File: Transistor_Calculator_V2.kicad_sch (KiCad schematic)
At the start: 51 parts, among them Q1 2N3904, Q10 2N3904, Q11 2N3904, Q12 2N3904, Q13 2N3904, Q14 2N3904, Q15 2N3904, Q16 2N3904, Q17 2N3904, Q18 2N3904, Q19 2N3904, Q2 2N3904, Q3 2N3904, Q4 2N3904, Q5 2N3904, Q6 2N3904, Q7 2N3904, Q8 2N3904, Q9 2N3904

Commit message: update transistors
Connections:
- net GND: now also Q1.1 (E), Q10.1 (E), Q12.1 (E), Q13.1 (E), Q15.1 (E), Q16.1 (E), Q17.1 (E), Q18.1 (E), Q19.1 (E), Q4.1 (E), Q5.1 (E), Q6.1 (E), Q9.1 (E)
- net Vcc: now also R12.2, R14.2, R15.1, R16.2, R17.2, R20.2, R23.2, R24.2, R27.2, R28.2, R4.2, R5.2, R7.2, R8.2
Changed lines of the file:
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@@
 	)
 	(junction
+		(at 127 31.75)
+		(diameter 0)
+		(color 0 0 0 0)
+	)
+	(junction
 		(at 236.22 133.35)
 		(diameter 0)
@@
 	)
 	(junction
+		(at 132.08 191.77)
+		(diameter 0)
+		(color 0 0 0 0)
+	)
+	(junction
 		(at 72.39 85.09)
 		(diameter 0)
@@
 	(wire
 		(pts
+			(xy 127 20.32) (xy 127 31.75)
+		)
+		(stroke
+			(width 0)
+			(type default)
+		)
+	)
+	(wire
+		(pts
 			(xy 58.42 157.48) (xy 58.42 162.56)
 		)
@@
 	(wire
 		(pts
+			(xy 132.08 191.77) (xy 121.92 191.77)
+		)
+		(stroke
+			(width 0)
+			(type default)
+		)
+	)
+	(wire
+		(pts
 			(xy 43.18 167.64) (xy 31.75 167.64)
 		)
@@
 	(wire
 		(pts
-			(xy 175.26 191.77) (xy 121.92 191.77)
+			(xy 175.26 191.77) (xy 132.08 191.77)
 		)
 		(stroke
@@
 	(wire
 		(pts
-			(xy 121.92 31.75) (xy 186.69 31.75)
+			(xy 121.92 31.75) (xy 127 31.75)
 		)
 		(stroke
@@
 	(wire
 		(pts
+			(xy 132.08 191.77) (xy 132.08 195.58)
+		)
+		(stroke
+			(width 0)
+			(type default)
+		)
+	)
+	(wire
+		(pts
+			(xy 135.89 20.32) (xy 127 20.32)
+		)
+		(stroke
+			(width 0)
+			(type default)
+		)
+	)
+	(wire
+		(pts
 			(xy 121.92 182.88) (xy 121.92 191.77)
 		)
@@
 	(wire
 		(pts
+			(xy 127 31.75) (xy 186.69 31.75)
+		)
+		(stroke
+			(width 0)
+			(type default)
+		)
+	)
+	(wire
+		(pts
 			(xy 161.29 85.09) (xy 179.07 85.09)
 		)
@@
 	(wire
 		(pts
+			(xy 143.51 195.58) (xy 132.08 195.58)
+		)
+		(stroke
+			(width 0)
+			(type default)
+		)
+	)
+	(wire
+		(pts
 			(xy 91.44 39.37) (xy 100.33 39.37)
 		)
@@
 		)
 	)
+	(global_label "Vcc"
+		(shape input)
+		(at 135.89 20.32 0)
+		(fields_autoplaced yes)
+		(effects
+			(font
+				(size 1.27 1.27)
+			)
+			(justify left)
+		)
+		(property "Intersheetrefs" "${INTERSHEET_REFS}"
+			(at 142.141 20.32 0)
+			(effects
+				(font
+					(size 1.27 1.27)
+				)
+				(justify left)
+				(hide yes)
+			)
+		)
+	)
 	(symbol
 		(lib_id "Transistor_BJT:2N3904")
@@
 			)
 		)
-		(property "Sim.Pins" "1=C 2=B 3=E"
+		(property "Sim.Pins" "1=E 2=B 3=C"
 			(at 69.85 41.91 0)
 			(effects
@@
 	)
 	(symbol
+		(lib_id "power:GND")
+		(at 143.51 195.58 90)
+		(unit 1)
+		(exclude_from_sim no)
+		(in_bom yes)
+		(on_board yes)
+		(dnp no)
+		(fields_autoplaced yes)
+		(property "Reference" "#PWR05"
+			(at 149.86 195.58 0)
+			(effects
+				(font
+					(size 1.27 1.27)
+				)
+				(hide yes)
+			)
+		)
+		(property "Value" "GND"
+			(at 148.59 195.58 0)
+			(effects
+				(font
+					(size 1.27 1.27)
+				)
+			)
+		)
+		(property "Footprint" ""
+			(at 143.51 195.58 0)
+			(effects
+				(font
+					(size 1.27 1.27)
+				)
+				(hide yes)
+			)
+		)
+		(property "Datasheet" ""
+			(at 143.51 195.58 0)
+			(effects
+				(font
+					(size 1.27 1.27)
+				)
+				(hide yes)
+			)
+		)
+		(property "Description" "Power symbol creates a global label with name \"GND\" , ground"
+			(at 143.51 195.58 0)
+			(effects
+				(font
+					(size 1.27 1.27)
+				)
+				(hide yes)
+			)
+		)
+		(pin "1"
+		)
+		(instances
+			(project "Transistor_Calculator_V2"
+				(path "/4e74c2aa-3410-4407-95d8-73d62854742b"
+					(reference "#PWR05")
+					(unit 1)
+				)
+			)
+		)
+	)
+	(symbol
 		(lib_id "Transistor_BJT:2N3904")
 		(at 55.88 167.64 0)
@@
 			)
 		)
-		(property "Sim.Pins" "1=C 2=B 3=E"
+		(property "Sim.Pins" "1=E 2=B 3=C"
 			(at 69.85 80.01 0)
 			(effects

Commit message: renamed vinc
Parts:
- Vin1: value 0 -> 5
- renumbered Vinc1 to Vinc
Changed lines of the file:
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@@
 			)
 		)
-		(property "Value" "0"
+		(property "Value" "5"
 			(at -68.58 101.4701 0)
 			(effects
@@
 		(dnp no)
 		(fields_autoplaced yes)
-		(property "Reference" "Vinc1"
+		(property "Reference" "Vinc"
 			(at -36.83 98.9301 0)
 			(effects
@@
 			(project "Transistor_Calculator_V2"
 				(path "/4e74c2aa-3410-4407-95d8-73d62854742b"
-					(reference "Vinc1")
-					(unit 1)
-				)
+					(reference "Vinc")
+					(unit 1)
+				)

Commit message: Fixed the carry bit problem for the schematic
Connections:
- net Vo2: no longer Q13.3 (C), Q16.3 (C), R16.1, R24.1, R25.1, R26.1
- new net: Q16.3 (C), R24.1, R25.1
- new net: Q13.3 (C), R16.1, R26.1
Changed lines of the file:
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@@
-	)
-	(junction
-		(at 165.1 135.89)
-		(diameter 0)
-		(color 0 0 0 0)
 	)
 	(junction
@@
 	)
 	(junction
-		(at 153.67 156.21)
-		(diameter 0)
-		(color 0 0 0 0)
-	)
-	(junction
 		(at 100.33 85.09)
 		(diameter 0)
@@
 	)
 	(junction
-		(at 152.4 144.78)
-		(diameter 0)
-		(color 0 0 0 0)
-	)
-	(junction
 		(at 72.39 50.8)
 		(diameter 0)
@@
 	)
 	(junction
-		(at 236.22 133.35)
-		(diameter 0)
-		(color 0 0 0 0)
-	)
-	(junction
 		(at 58.42 162.56)
 		(diameter 0)
@@
 	(wire
 		(pts
-			(xy 152.4 144.78) (xy 175.26 144.78)
+			(xy 143.51 144.78) (xy 175.26 144.78)
 		)
 		(stroke
@@
 	(wire
 		(pts
-			(xy 152.4 144.78) (xy 152.4 142.24)
-		)
-		(stroke
-			(width 0)
-			(type default)
-		)
-	)
-	(wire
-		(pts
 			(xy 107.95 85.09) (xy 161.29 85.09)
 		)
@@
 	(wire
 		(pts
-			(xy 143.51 144.78) (xy 152.4 144.78)
-		)
-		(stroke
-			(width 0)
-			(type default)
-		)
-	)
-	(wire
-		(pts
-			(xy 165.1 121.92) (xy 236.22 121.92)
-		)
-		(stroke
-			(width 0)
-			(type default)
-		)
-	)
-	(wire
-		(pts
 			(xy 254 39.37) (xy 254 113.03)
 		)
@@
 	(wire
 		(pts
-			(xy 170.18 142.24) (xy 170.18 135.89)
-		)
-		(stroke
-			(width 0)
-			(type default)
-		)
-	)
-	(wire
-		(pts
 			(xy 252.73 115.57) (xy 252.73 133.35)
 		)
@@
 	(wire
 		(pts
-			(xy 236.22 121.92) (xy 236.22 133.35)
-		)
-		(stroke
-			(width 0)
-			(type default)
-		)
-	)
-	(wire
-		(pts
 			(xy 190.5 134.62) (xy 190.5 138.43)
 		)
@@
 	(wire
 		(pts
-			(xy 165.1 121.92) (xy 165.1 135.89)
-		)
-		(stroke
-			(width 0)
-			(type default)
-		)
-	)
-	(wire
-		(pts
 			(xy 190.5 161.29) (xy 201.93 161.29)
 		)
@@
 	(wire
 		(pts
-			(xy 151.13 156.21) (xy 151.13 135.89)
-		)
-		(stroke
-			(width 0)
-			(type default)
-		)
-	)
-	(wire
-		(pts
 			(xy 198.12 39.37) (xy 198.12 54.61)
 		)
@@
 	(wire
 		(pts
-			(xy 215.9 133.35) (xy 236.22 133.35)
+			(xy 215.9 133.35) (xy 252.73 133.35)
 		)
 		(stroke
@@
 	(wire
 		(pts
-			(xy 236.22 133.35) (xy 252.73 133.35)
-		)
-		(stroke
-			(width 0)
-			(type default)
-		)
-	)
-	(wire
-		(pts
 			(xy 127 72.39) (xy 127 105.41)
 		)
@@
 	(wire
 		(pts
-			(xy 153.67 156.21) (xy 151.13 156.21)
-		)
-		(stroke
-			(width 0)
-			(type default)
-		)
-	)
-	(wire
-		(pts
 			(xy 180.34 38.1) (xy 180.34 39.37)
 		)
@@
 	(wire
 		(pts
-			(xy 151.13 135.89) (xy 165.1 135.89)
-		)
-		(stroke
-			(width 0)
-			(type default)
-		)
-	)
-	(wire
-		(pts
 			(xy 207.01 44.45) (xy 207.01 39.37)
 		)
@@
 	(wire
 		(pts
-			(xy 165.1 135.89) (xy 170.18 135.89)
-		)
-		(stroke
-			(width 0)
-			(type default)
-		)
-	)
-	(wire
-		(pts
 			(xy 170.18 50.8) (xy 170.18 54.61)
 		)
@@
 		)
 		(stroke
-			(width 0)
-			(type default)
-		)
-	)
-	(wire
-		(pts
-			(xy 152.4 142.24) (xy 170.18 142.24)
-		)
-		(stroke

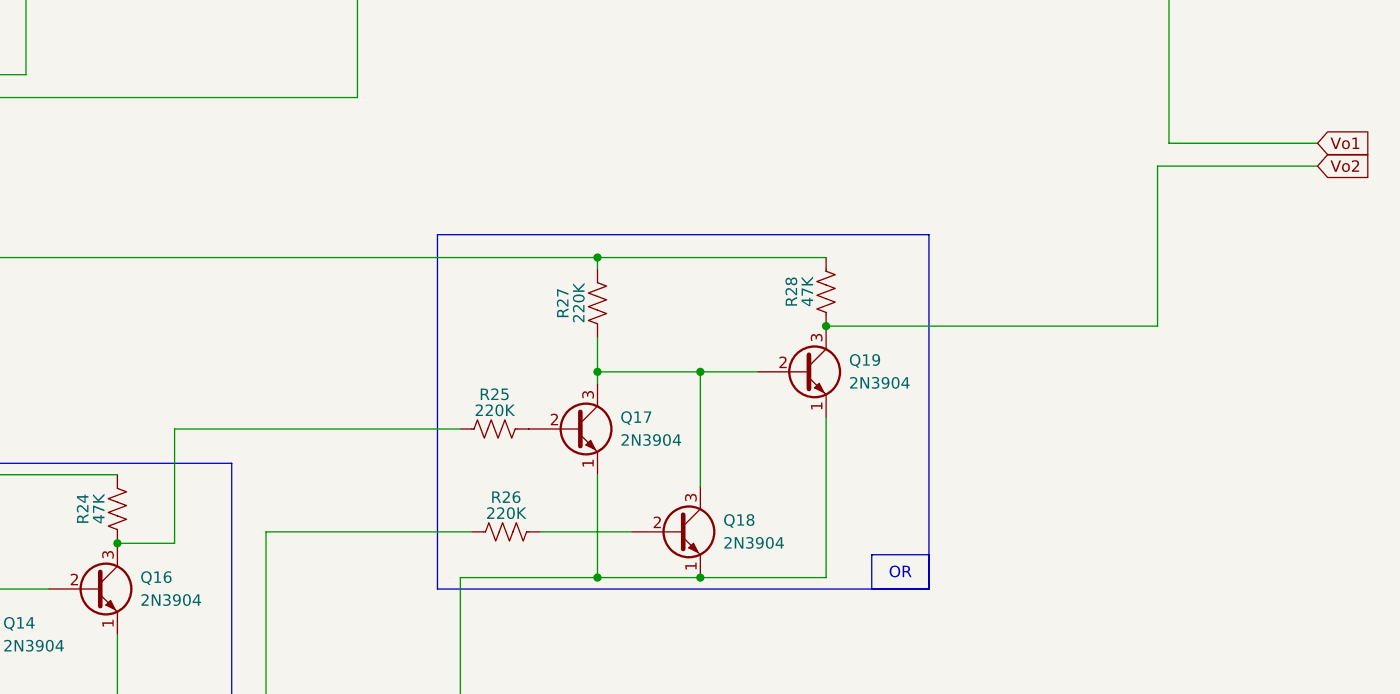
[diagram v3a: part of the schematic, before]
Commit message: Added diode to replace OR gate
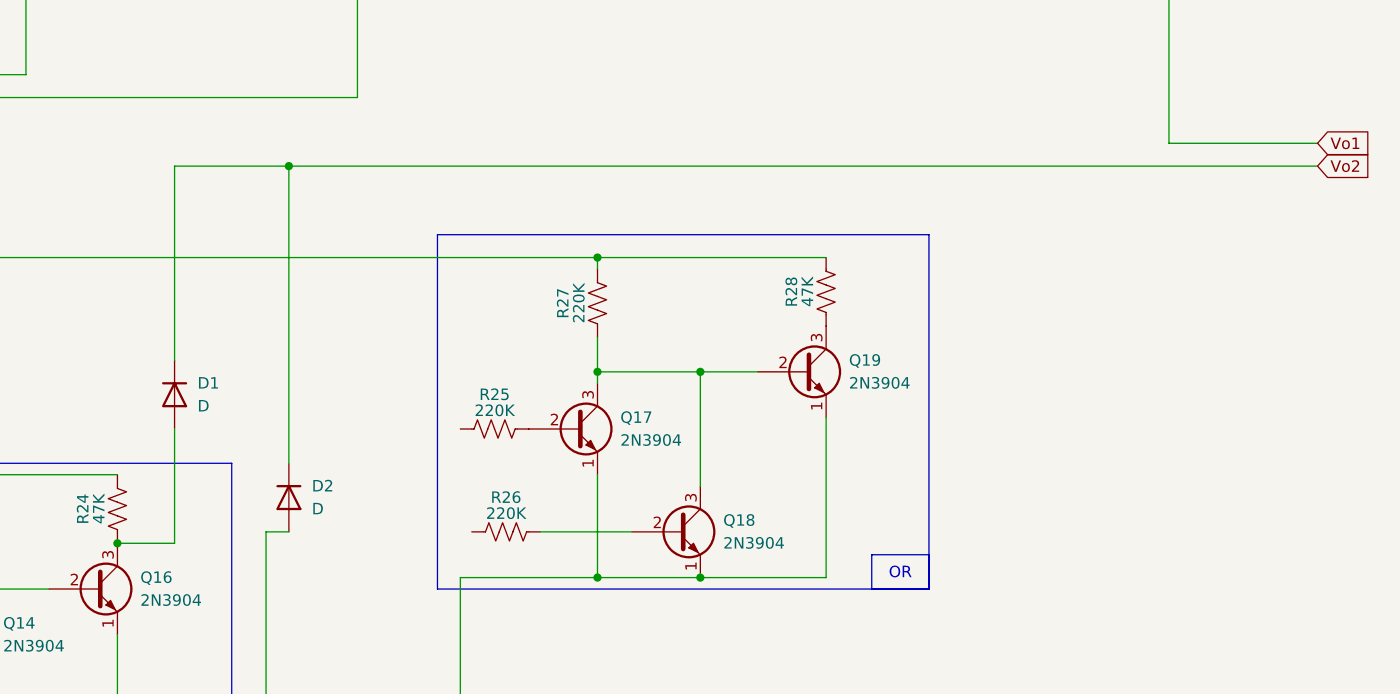
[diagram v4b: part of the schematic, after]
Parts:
- added D1, D2: D, symbol Device:D
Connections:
- net Vo2: now also D1.1 (K), D2.1 (K); no longer Q19.3 (C), R28.1
- net at Q16.3 (C), R24.1: now also D1.2 (A); no longer R25.1
- net at Q13.3 (C), R16.1: now also D2.2 (A); no longer R26.1
- new net: Q19.3 (C), R28.1
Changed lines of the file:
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@@
 	)
 	(junction
+		(at 156.21 115.57)
+		(diameter 0)
+		(color 0 0 0 0)
+	)
+	(junction
 		(at 161.29 85.09)
 		(diameter 0)
@@
 	)
 	(junction
-		(at 215.9 133.35)
-		(diameter 0)
-		(color 0 0 0 0)
-	)
-	(junction
 		(at 198.12 39.37)
 		(diameter 0)
@@
 	(wire
 		(pts
-			(xy 143.51 144.78) (xy 175.26 144.78)
-		)
-		(stroke
-			(width 0)
-			(type default)
-		)
-	)
-	(wire
-		(pts
 			(xy 72.39 85.09) (xy 100.33 85.09)
 		)
@@
 	(wire
 		(pts
+			(xy 143.51 115.57) (xy 156.21 115.57)
+		)
+		(stroke
+			(width 0)
+			(type default)
+		)
+	)
+	(wire
+		(pts
 			(xy 72.39 50.8) (xy 72.39 74.93)
 		)
@@
 	(wire
 		(pts
-			(xy 252.73 115.57) (xy 252.73 133.35)
-		)
-		(stroke
-			(width 0)
-			(type default)
-		)
-	)
-	(wire
-		(pts
 			(xy 127 72.39) (xy 146.05 72.39)
 		)
@@
 	(wire
 		(pts
-			(xy 215.9 133.35) (xy 252.73 133.35)
-		)
-		(stroke
-			(width 0)
-			(type default)
-		)
-	)
-	(wire
-		(pts
 			(xy 161.29 64.77) (xy 161.29 67.31)
 		)
@@
 	(wire
 		(pts
+			(xy 156.21 115.57) (xy 156.21 148.59)
+		)
+		(stroke
+			(width 0)
+			(type default)
+		)
+	)
+	(wire
+		(pts
 			(xy 66.04 162.56) (xy 58.42 162.56)
 		)
@@
 	(wire
 		(pts
+			(xy 143.51 137.16) (xy 143.51 115.57)
+		)
+		(stroke
+			(width 0)
+			(type default)
+		)
+	)
+	(wire
+		(pts
 			(xy 207.01 44.45) (xy 207.01 39.37)
 		)
@@
 	(wire
 		(pts
+			(xy 156.21 115.57) (xy 270.51 115.57)
+		)
+		(stroke
+			(width 0)
+			(type default)
+		)
+	)
+	(wire
+		(pts
 			(xy 148.59 43.18) (xy 171.45 43.18)
 		)
@@
 	(wire
 		(pts
-			(xy 153.67 156.21) (xy 176.53 156.21)
+			(xy 153.67 156.21) (xy 156.21 156.21)
 		)
 		(stroke
@@
 	(wire
 		(pts
-			(xy 270.51 115.57) (xy 252.73 115.57)
-		)
-		(stroke
-			(width 0)
-			(type default)
-		)
-	)
-	(wire
-		(pts
 			(xy 80.01 50.8) (xy 80.01 64.77)
 		)
@@
 	)
 	(symbol
+		(lib_id "Device:D")
+		(at 143.51 140.97 270)
+		(unit 1)
+		(exclude_from_sim no)
+		(in_bom yes)
+		(on_board yes)
+		(dnp no)
+		(fields_autoplaced yes)
+		(property "Reference" "D1"
+			(at 146.05 139.6999 90)
+			(effects
+				(font
+					(size 1.27 1.27)
+				)
+				(justify left)
+			)
+		)
+		(property "Value" "D"
+			(at 146.05 142.2399 90)
+			(effects
+				(font
+					(size 1.27 1.27)
+				)
+				(justify left)
+			)
+		)
+		(property "Footprint" ""
+			(at 143.51 140.97 0)
+			(effects
+				(font
+					(size 1.27 1.27)
+				)
+				(hide yes)
+			)
+		)
+		(property "Datasheet" "~"
+			(at 143.51 140.97 0)
+			(effects
+				(font
+					(size 1.27 1.27)
+				)
+				(hide yes)
+			)
+		)
+		(property "Description" "Diode"
+			(at 143.51 140.97 0)
+			(effects
+				(font
+					(size 1.27 1.27)
+				)
+				(hide yes)
+			)
+		)
+		(property "Sim.Device" "D"
+			(at 143.51 140.97 0)
+			(effects
+				(font
+					(size 1.27 1.27)
+				)
+				(hide yes)
+			)
+		)
+		(property "Sim.Pins" "1=K 2=A"
+			(at 143.51 140.97 0)
+			(effects
+				(font
+					(size 1.27 1.27)
+				)
+				(hide yes)
+			)
+		)
+		(pin "1"
+		)
+		(pin "2"
+		)
+		(instances
+			(project "Transistor_Calculator_V2"
+				(path "/4e74c2aa-3410-4407-95d8-73d62854742b"
+					(reference "D1")
+					(unit 1)
+				)
+			)
+		)
+	)
+	(symbol
 		(lib_id "Simulation_SPICE:VDC")
 		(at -73.66 100.33 0)
@@
 					(unit 1)
 				)
+			)
+		)
+	)
+	(symbol
+		(lib_id "Device:D")
+		(at 156.21 152.4 270)
+		(unit 1)
+		(exclude_from_sim no)
+		(in_bom yes)
+		(on_board yes)
+		(dnp no)
+		(fields_autoplaced yes)
+		(property "Reference" "D2"
+			(at 158.75 151.1299 90)
+			(effects
+				(font
+					(size 1.27 1.27)
+				)
+				(justify left)
+			)
+		)
+		(property "Value" "D"
+			(at 158.75 153.6699 90)
+			(effects
+				(font
+					(size 1.27 1.27)
+				)
+				(justify left)
+			)
+		)
+		(property "Footprint" ""
+			(at 156.21 152.4 0)
+			(effects
+				(font
+					(size 1.27 1.27)
+				)
+				(hide yes)
+			)
+		)
+		(property "Datasheet" "~"
+			(at 156.21 152.4 0)
+			(effects
+				(font
+					(size 1.27 1.27)
+				)
+				(hide yes)
+			)
+		)
+		(property "Description" "Diode"
+			(at 156.21 152.4 0)
+			(effects
+				(font
+					(size 1.27 1.27)
+				)
+				(hide yes)
+			)
+		)
+		(property "Sim.Device" "D"
+			(at 156.21 152.4 0)
+			(effects
+				(font
+					(size 1.27 1.27)
+				)
+				(hide yes)
+			)
+		)
+		(property "Sim.Pins" "1=K 2=A"
+			(at 156.21 152.4 0)
+			(effects
+				(font
+					(size 1.27 1.27)
+				)
+				(hide yes)
+			)
+		)
+		(pin "1"
+		)
+		(pin "2"
+		)
+		(instances
+			(project "Transistor_Calculator_V2"
+				(path "/4e74c2aa-3410-4407-95d8-73d62854742b"
+					(reference "D2")
+					(unit 1)
+				)
